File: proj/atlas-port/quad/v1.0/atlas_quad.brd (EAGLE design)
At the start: 123.2 x 21.6 mm, 30 parts, among them J1 Atlas Stamp, J2 5227161-9, J3 I2C-HEADER, J4 5227161-9, J5 Atlas Stamp, J6 I2C-HEADER, U1 ISO1540, U2 RM-3.33.3S, U3 ISO1540, U4 RM-3.33.3S

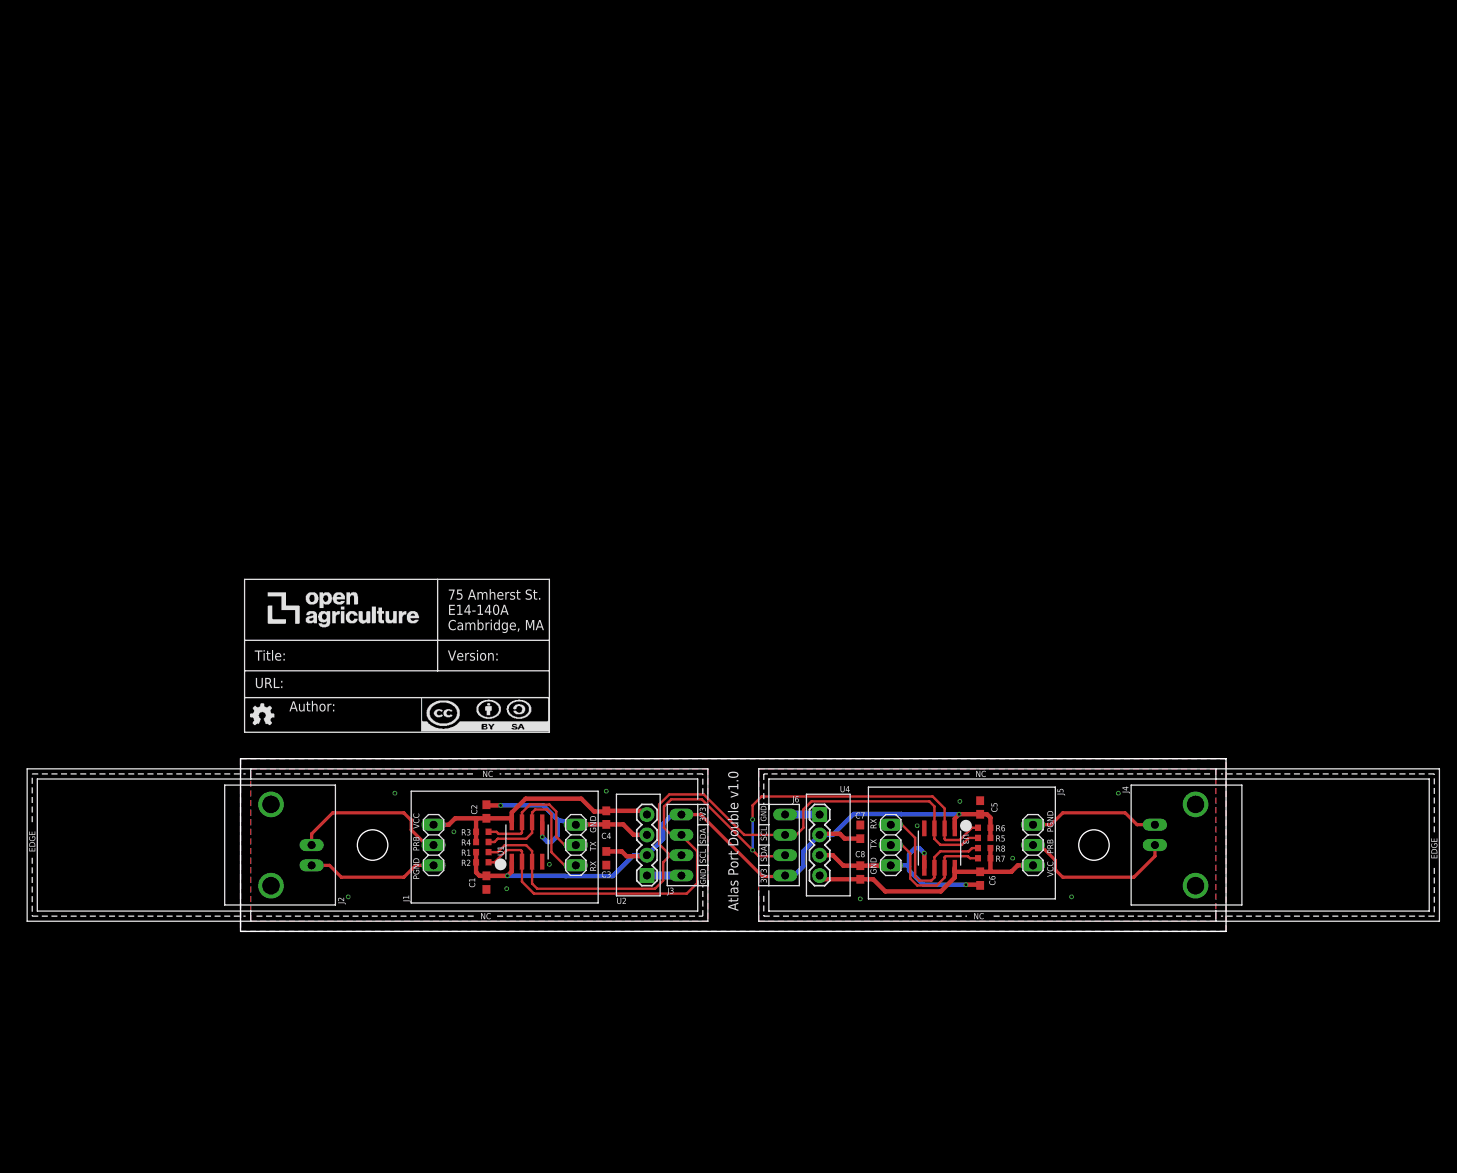
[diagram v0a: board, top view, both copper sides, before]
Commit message: added atlas sensor port quad v1.0
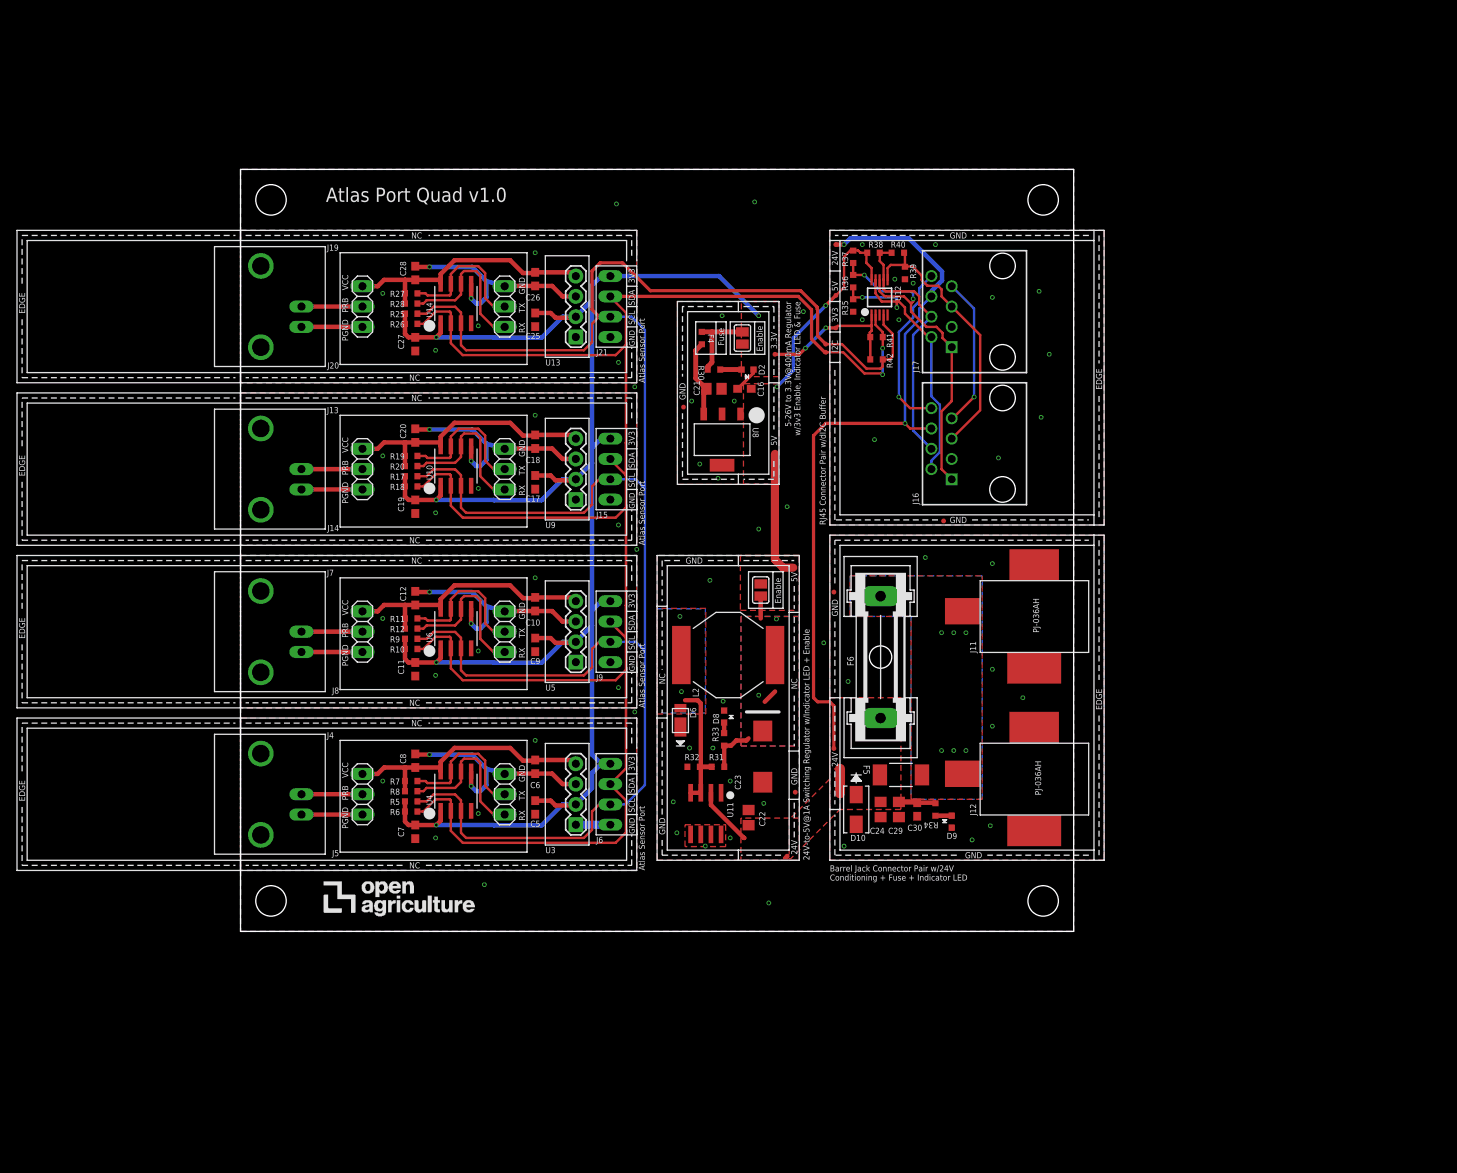
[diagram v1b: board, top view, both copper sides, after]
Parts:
- removed C1, C2, C3, C4: 0.1uF, openag-capacitors:C0603
- removed J1: Atlas Stamp, openag-connectors:ATLAS-STAMP
- removed J2: 5227161-9, openag-connectors:BNC
- removed J3: I2C-HEADER, openag-connectors:OPENAG-I2C-HEADER
- removed R1, R2, R3, R4: 1K, openag-resistors:RC0603N
- removed U1: ISO1540, openag-isolators:D8
- removed U2: RM-3.33.3S, openag-isolators:SIP4
- added C10, C11, C12, C16, C17, C18, C19, C20, C25, C26, C27, C28, C30, C9: 0.1uF, openag-capacitors:C0603
- added C21, C24: 10uF, openag-capacitors:C0805
- added C22: 15uF, openag-capacitors:C0805
- added C23: 220uF, openag-capacitors:CT7343
- added C29: 4.7uF, openag-capacitors:C0805
- added D10: SMAJ26A, openag-diodes:SMA
- added D2, D8, D9: APT1608, openag-diodes:CHIPLED_0603
- added D6: SBR2A40P1-7, openag-diodes:POWERDI123
- added F4: 0448.400MR, openag-fuses:0603
- added F5: SST 7, openag-fuses:SS
- added F6: (no value), fuse:GSH15
- added J11, J12: PJ-036AH, openag-connectors:PJ-036AH
- added J13, J19, J7: 5227161-9, openag-connectors:BNC
- added J14, J20, J8: Atlas Stamp, openag-connectors:ATLAS-STAMP
- added J15, J21, J9: I2C-HEADER, openag-connectors:OPENAG-I2C-HEADER
- added J16, J17: 54602-908LF, openag_connector:OPENAG-V1-RJ45
- added L2: 68uH, openag-inductors:UP2B
- added R10, R11, R12, R17, R18, R19, R20, R25, R26, R27, R28, R9: 1K, openag-resistors:RC0603N
- added R30, R33, R34: 100, openag-resistors:RC0603N
- added R31: 3.01K, openag-resistors:RC0603N
- added R32: 976 Ohm, openag-resistors:RC0603N
- added R35, R37, R38, R39: 600, openag-resistors:RC0603N
- added R36, R40: 120, openag-resistors:RC0603N
- added R41, R42: 10K, openag-resistors:RC0603N
- added SJ1, SJ4: (no value), openag-connectors:SOLDERJUMPER_REFLOW_NOPASTE
- added TP1, TP10, TP11, TP12, TP13, TP14, TP15, TP16, TP17, TP18, TP2, TP3, TP8, TP9: TPTP06R, openag-testpads:TP06R
- added U$1, U$4: (no value), openag-frames:OPENAG-CORNER-MOUNTING-HOLE
- added U10, U14, U6: ISO1540, openag-isolators:D8
- added U11: MIC4680YM-TR, openag-regulators:SOIC8
- added U12: PCA9615DPJ, openag-buffers:SOP50P490X110-10N
- added U13, U5, U9: RM-3.33.3S, openag-isolators:SIP4
- added U8: LM2937IMP3.3NOPB, openag-regulators:MP04A
- U3: value ISO1540 -> RM-3.33.3S; device openag-isolators:D8 -> openag-isolators:SIP4
- U4: value RM-3.33.3S -> ISO1540; device openag-isolators:SIP4 -> openag-isolators:D8
- moved J4 117.0 mm to (2.54, 17.1), turned to 90 degrees
- moved R7 72.3 mm to (21.3, 18.8), turned to 180 degrees
- moved R8 72.0 mm to (21.3, 17.5), turned to 180 degrees
- moved R5 71.8 mm to (21.3, 16.3), turned to 180 degrees
- moved R6 71.7 mm to (21.3, 15.0), turned to 180 degrees
- moved J5 66.3 mm to (24.1, 17.1), turned to 180 degrees
- moved FRAME1 57.8 mm to (52.8, 49.5), flipped to the bottom, turned to 90 degrees
- moved C6 57.4 mm to (36.8, 20.6)
- moved C8 57.4 mm to (21.8, 21.3)
- moved C5 55.6 mm to (36.8, 15.5), turned to 270 degrees
- moved C7 55.6 mm to (21.8, 12.4), turned to 270 degrees
- moved U$5 49.3 mm to (10.4, 2.29), flipped to the top, turned to 0 degrees
- moved U3 45.6 mm to (41.9, 13.3), turned to 90 degrees
- moved U4 45.6 mm to (26.9, 17.5), turned to 90 degrees
- moved J6 21.3 mm to (47.0, 17.1), turned to 90 degrees
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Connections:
- new net +24V: C22.1, C24.1, C29.1, C30.1, D10.1, F5.2, F6.2, J16.24V(6), J17.24V(6), R34.2, TP10.TP, TP12.TP, TP18.TP, U11.2
- new net +5V: C16.1, R37.1, R38.2, SJ4.2, TP17.TP, TP2.TP, TP8.TP, U12.10, U8.1
- new net 24V_IN: F5.1, F6.1, J11.1, J12.1
- new net DSCLM: J16.DSCLM(5), J17.DSCLM(5), R39.2, R40.1, U12.6
- new net DSCLP: J16.DSCLP(4), J17.DSCLP(4), R38.1, R40.2, U12.7
- new net DSDAM: J16.DSDAM(2), J17.DSDAM(2), R35.1, R36.2, U12.9
- new net DSDAP: J16.DSDAP(1), J17.DSDAP(1), R36.1, R37.2, U12.8
- new net ISO_3V3_3: C18.1, C20.1, J14.4, R19.2, R20.2, U10.8, U9.4
- new net ISO_3V3_4: C26.1, C28.1, J20.4, R27.2, R28.2, U13.4, U14.8
- new net ISO_GND_3: C18.2, C20.2, J14.3, U10.5, U9.3
- new net ISO_GND_4: C26.2, C28.2, J20.3, U13.3, U14.5
- new net ISO_SCL_3: J14.1, R20.1, U10.6
- new net ISO_SCL_4: J20.1, R28.1, U14.6
- new net ISO_SDA_3: J14.2, R19.1, U10.7
- new net ISO_SDA_4: J20.2, R27.1, U14.7
- new net N$11: D6.+, L2.1, R31.1, R32.2, U11.3, U11.4
- new net N$27: D8.A, R33.1
- new net N$45: C23.+, L2.2, R31.2, R33.2, SJ4.1
- new net N$46: D9.A, R34.1
- new net N$6: D2.A, R30.1
- new net N$8: C21.1, F4.1, U8.3
- new net PGND_3: J13.GND, J14.6
- new net PGND_4: J19.GND, J20.6
- new net PRB_3: J13.S, J14.5
- new net PRB_4: J19.S, J20.5
- new net REG_3V3_400MA: F4.2, R30.2, SJ1.1
- new net USBM: J16.USBM(8), J17.USBM(8)
- new net USBP: J16.USBP(7), J17.USBP(7)
- net +3V3: now also C11.1, C17.1, C19.1, C25.1, C27.1, C9.1, J15.3V3, J21.3V3, J9.3V3, R10.2, R17.2, R18.2, R25.2, R26.2, R41.2, R42.2, R9.2, SJ1.2, TP15.TP, TP3.TP, U10.1, U12.1, U13.2, U14.1, U3.2, U4.1, U5.2, U6.1, U9.2; no longer C1.1, C3.1, J3.3V3, R1.2, R2.2, U1.1, U2.2, U3.1, U4.2
- net GND: now also C11.2, C16.2, C17.2, C19.2, C21.2, C22.2, C23.-, C24.2, C25.2, C27.2, C29.2, C30.2, C9.2, D10.2, D2.C, D6.-, D8.C, D9.C, J11.2, J11.3, J12.2, J12.3, J15.GND, J16.GND(3), J17.GND(3), J21.GND, J9.GND, R32.1, R35.2, R39.1, TP1.TP, TP11.TP, TP16.TP, TP9.TP, U10.4, U11.1, U11.5, U11.6, U11.7, U11.8, U12.5, U13.1, U14.4, U3.1, U4.4, U5.1, U6.4, U8.2, U8.4, U9.1; no longer C1.2, C3.2, J3.GND, U1.4, U2.1, U3.4, U4.1
- net ISO_3V3_1: now also C6.1, C8.1, J5.4, R7.2, R8.2, U3.4, U4.8; no longer C2.1, C4.1, J1.4, R3.2, R4.2, U1.8, U2.4
- net ISO_3V3_2: now also C10.1, C12.1, J8.4, R11.2, R12.2, U5.4, U6.8; no longer C6.1, C8.1, J5.4, R7.2, R8.2, U3.8, U4.4
- net ISO_GND_1: now also C6.2, C8.2, J5.3, U3.3, U4.5; no longer C2.2, C4.2, J1.3, U1.5, U2.3
- net ISO_GND_2: now also C10.2, C12.2, J8.3, U5.3, U6.5; no longer C6.2, C8.2, J5.3, U3.5, U4.3
- net ISO_SCL_1: now also J5.1, R8.1, U4.6; no longer J1.1, R4.1, U1.6
- net ISO_SCL_2: now also J8.1, R12.1, U6.6; no longer J5.1, R8.1, U3.6
- net ISO_SDA_1: now also J5.2, R7.1, U4.7; no longer J1.2, R3.1, U1.7
- net ISO_SDA_2: now also J8.2, R11.1, U6.7; no longer J5.2, R7.1, U3.7
- net PGND_1: now also J4.GND, J5.6; no longer J1.6, J2.GND
- net PGND_2: now also J7.GND, J8.6; no longer J4.GND, J5.6
- net PRB_1: now also J4.S, J5.5; no longer J1.5, J2.S
- net PRB_2: now also J7.S, J8.5; no longer J4.S, J5.5
- net SCL: now also J15.SCL, J21.SCL, J9.SCL, R17.1, R25.1, R42.1, R9.1, TP13.TP, U10.3, U12.4, U14.3, U4.3, U6.3; no longer J3.SCL, R1.1, U1.3, U3.3
- net SDA: now also J15.SDA, J21.SDA, J9.SDA, R10.1, R18.1, R26.1, R41.1, TP14.TP, U10.2, U12.2, U14.2, U4.2, U6.2; no longer J3.SDA, R2.1, U1.2, U3.2
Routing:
- net SCL: track 89.6 -> 263.9 mm
- net +3V3: track 96.6 -> 255.2 mm, vias 2 -> 7
- net SDA: track 101.6 -> 250.1 mm
- net +24V: track 0.00 -> 108.5 mm, vias 0 -> 2
- net DSDAP: track 0.00 -> 43.2 mm, vias 0 -> 2
- net +5V: track 0.00 -> 42.7 mm, vias 0 -> 2
- net DSDAM: track 0.00 -> 38.1 mm, vias 0 -> 2
- net DSCLM: track 0.00 -> 33.9 mm
- net ISO_3V3_3: track 0.00 -> 33.3 mm
- net ISO_3V3_4: track 0.00 -> 33.3 mm
- net DSCLP: track 0.00 -> 32.7 mm
- net ISO_GND_3: track 0.00 -> 27.8 mm, vias 0 -> 2
- net ISO_GND_4: track 0.00 -> 27.8 mm, vias 0 -> 2
- net USBM: track 0.00 -> 21.4 mm, vias 0 -> 1
- net ISO_SCL_3: track 0.00 -> 19.8 mm
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- added copper zone on layer 1, net +24V
- added copper zone on layer 1, net +3V3
- added copper zone on layer 1, net +5V
- added copper zone on layer 1, net 24V_IN
- added copper zone on layer 16, net 24V_IN
- added copper zone on layer 1, net N$11
- added copper zone on layer 16, net N$11
- added copper zone on layer 1, net N$45
- added copper zone on layer 16, net N$45
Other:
- board size 123.2 x 21.6 mm -> 104.1 x 95.2 mm
- board text added: "24V"
- board text added: "24V-to-5V@1A Switching Regulator w/Indicator LED + Enable"
- board text added: "3.3V"
- board text added: "3V3"
- board text added: "5-26V to 3.3V@400mA Regulator w/3v3 Enable, Indicator LED & Fuse"
- board text added: "5V"
- board text added: "Atlas Port Quad v1.0"
- board text added: "Atlas Sensor Port"
- board text added: "Barrel Jack Connector Pair w/24V Conditioning + Fuse + Indicator LED"
- board text added: "Enable"
- board text added: "Fuse"
- board text added: "GND"
- board text added: "I2C"
- board text added: "RJ45 Connector Pair w/dI2C Buffer"
- board text removed: "Atlas Port Double v1.0"

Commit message: updated atlas port quad v1.0 manufacturing files
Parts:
- F5: value SST 7 -> SST7
- F6: device fuse:GSH15 -> openag-fuses:GSH15
- J16, J17: device openag_connector:OPENAG-V1-RJ45 -> openag-connectors:OPENAG-V1-RJ45
- U11: value MIC4680YM-TR -> MIC4680
- U12: value PCA9615DPJ -> PCA9615
- U8: value LM2937IMP3.3NOPB -> LM2937

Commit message: added photon quad v1.0 at 90%
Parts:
- removed C29: 4.7uF, openag-capacitors:C0805
- removed C30, C8: 0.1uF, openag-capacitors:C0603
- removed D10: SMAJ26A, openag-diodes:SMA
- removed D8, D9: APT1608, openag-diodes:CHIPLED_0603
- removed F4: 0448.400MR, openag-fuses:0603
- removed F5: SST7, openag-fuses:SS
- removed F6: (no value), openag-fuses:GSH15
- removed FRAME1: (no value), openag-frames:DOCFIELD
- removed J11, J12: PJ-036AH, openag-connectors:PJ-036AH
- removed J16, J17: 54602-908LF, openag-connectors:OPENAG-V1-RJ45
- removed R20: 1K, openag-resistors:RC0603N
- removed R30, R33, R34: 100, openag-resistors:RC0603N
- removed R31: 3.01K, openag-resistors:RC0603N
- removed R32: 976 Ohm, openag-resistors:RC0603N
- removed R35, R37, R38, R39: 600, openag-resistors:RC0603N
- removed R36, R40: 120, openag-resistors:RC0603N
- removed R41, R42: 10K, openag-resistors:RC0603N
- removed SJ4: (no value), openag-connectors:SOLDERJUMPER_REFLOW_NOPASTE
- removed TP16: TPTP06R, openag-testpads:TP06R
- removed U11: MIC4680, openag-regulators:SOIC8
- added C1, C14, C2, C3, C4: 0.1uF, openag-capacitors:C0603
- added C15: 10uF, openag-capacitors:C0805
- added D1, D4: APT1608, openag-diodes:CHIPLED_0603
- added D3: SMAJ26A, openag-diodes:SMA
- added F1, F2: SSQ5, openag-fuses:SS
- added J1: 5227161-9, openag-connectors:BNC-5227161
- added J10: 54602-908LF, openag-connectors:RJ45-DI2C-USB-54602-908LF
- added J2: I2C-HEADER, openag-connectors:HEADER-I2C
- added J3: ATLAS-STAMP, openag-connectors:ATLAS-STAMP
- added R1, R2, R23, R24: 2.2k, openag-resistors:RC0603N
- added R13: 1K, openag-resistors:RC0603N
- added R14, R15, R16, R3: 600, openag-resistors:RC0603N
- added R21, R22: 100, openag-resistors:RC0603N
- added R4: 120, openag-resistors:RC0603N
- added TP19, TP20, TP28, TP29, TP30, TP31, TP32, TP4, TP5, TP58, TP6, TP7, TP71, TP72, TP73: TPTP04R, openag-testpads:TP04R
- added TP23, TP24, TP25: TPTP06R, openag-testpads:TP06R
- added U$6: TITLE, openag-frames:TITLE
- added U$8: (no value), openag-frames:LOGO-900X300
- added U1: ISO1540, openag-isolators:D8
- added U2: RM-3.33.3S, openag-isolators:RM3.33.3S-SIP4
- added U7: LM2937-3.3V, openag-regulators:MP04A
- C20, C5: value 0.1uF -> 10uF; device openag-capacitors:C0603 -> openag-capacitors:C0805
- C22: value 15uF -> 10uF
- C23: value 220uF -> 0.1uF; device openag-capacitors:CT7343 -> openag-capacitors:C0603
- C24: value 10uF -> 0.1uF; device openag-capacitors:C0805 -> openag-capacitors:C0603
- C28, C6: value 0.1uF -> 4.7uF; device openag-capacitors:C0603 -> openag-capacitors:C0805
- D6: value SBR2A40P1-7 -> APT1608; device openag-diodes:POWERDI123 -> openag-diodes:CHIPLED_0603
- J13, J19, J7: value 5227161-9 -> ATLAS-STAMP; device openag-connectors:BNC -> openag-connectors:ATLAS-STAMP
- J14, J20, J8: value Atlas Stamp -> I2C-HEADER; device openag-connectors:ATLAS-STAMP -> openag-connectors:HEADER-I2C
- J15, J21, J9: value I2C-HEADER -> 5227161-9; device openag-connectors:OPENAG-I2C-HEADER -> openag-connectors:BNC-5227161
- J4: value 5227161-9 -> PJ-036AH; device openag-connectors:BNC -> openag-connectors:BARREL-JACK-PJ-036AH
- J5: value Atlas Stamp -> PJ-036AH; device openag-connectors:ATLAS-STAMP -> openag-connectors:BARREL-JACK-PJ-036AH
- J6: value I2C-HEADER -> 54602-908LF; device openag-connectors:OPENAG-I2C-HEADER -> openag-connectors:RJ45-DI2C-USB-54602-908LF
- L2: value 68uH -> 33uH; device openag-inductors:UP2B -> openag-inductors:29333C
- R10, R18, R19: value 1K -> 120
- R11, R12: value 1K -> 10K
- R17, R7, R8, R9: value 1K -> 600
- R25: value 1K -> 0 OHM
- R26: value 1K -> 100
- R27, R28, R5, R6: value 1K -> 2.2k
- SJ1: device openag-connectors:SOLDERJUMPER_REFLOW_NOPASTE -> openag-connectors:EMI-BYPASS
- TP1, TP10, TP11, TP12, TP13, TP14, TP15, TP17, TP18, TP2, TP3, TP8, TP9: value TPTP06R -> TPTP04R; device openag-testpads:TP06R -> openag-testpads:TP04R
- U$1, U$2, U$3, U$4: device openag-frames:OPENAG-CORNER-MOUNTING-HOLE -> openag-frames:CORNER-150
- U$5: value (none) -> AUTHOR; device openag-frames:OPENAG-LOGO-750-MIL -> openag-frames:AUTHOR
- U12: value PCA9615 -> PHOTONH; device openag-buffers:SOP50P490X110-10N -> openag-microcontrollers:PHOTON
- U13, U5, U9: device openag-isolators:SIP4 -> openag-isolators:RM3.33.3S-SIP4
- U3: value RM-3.33.3S -> PCA9615; device openag-isolators:SIP4 -> openag-buffers:SOP50P490X110-10N
- U4: value ISO1540 -> PCA9615; device openag-isolators:D8 -> openag-buffers:SOP50P490X110-10N
- U8: value LM2937 -> R-78E5.0-1.0; device openag-regulators:MP04A -> openag-regulators:R-78E5.0-1.0
- moved U$2 136.7 mm to (95.2, 105.4), turned to 180 degrees
- moved U$1 125.8 mm to (95.2, 5.08), turned to 90 degrees
- moved U$5 105.6 mm to (99.1, 59.7), turned to 90 degrees
- moved J4 99.8 mm to (61.0, 98.1), turned to 270 degrees
- moved J5 97.7 mm to (78.7, 98.1), turned to 270 degrees
- moved U$4 96.3 mm to (5.08, 105.4), turned to 270 degrees
- moved U$3 95.3 mm to (5.08, 5.08), turned to 0 degrees
- moved TP10 90.1 mm to (47.5, 97.1)
- moved J6 87.5 mm to (21.6, 100.9), turned to 180 degrees
- moved C7 84.5 mm to (69.3, 82.3)
- moved TP9 83.6 mm to (47.5, 98.1)
- moved TP12 82.9 mm to (47.5, 101.4), turned to 270 degrees
- moved J21 80.3 mm to (19.7, 2.54), turned to 180 degrees
- moved C5 76.3 mm to (73.7, 82.3)
- moved U3 76.2 mm to (23.1, 87.2), turned to 180 degrees
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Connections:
- removed net 24V_IN: F5.1, F6.1, J11.1, J12.1
- removed net DSCLM: J16.DSCLM(5), J17.DSCLM(5), R39.2, R40.1, U12.6
- removed net DSCLP: J16.DSCLP(4), J17.DSCLP(4), R38.1, R40.2, U12.7
- removed net DSDAM: J16.DSDAM(2), J17.DSDAM(2), R35.1, R36.2, U12.9
- removed net DSDAP: J16.DSDAP(1), J17.DSDAP(1), R36.1, R37.2, U12.8
- removed net N$27: D8.A, R33.1
- removed net N$45: C23.+, L2.2, R31.2, R33.2, SJ4.1
- removed net N$46: D9.A, R34.1
- removed net REG_3V3_400MA: F4.2, R30.2, SJ1.1
- new net 24V_EMI: C15.1, L2.2, SJ1.2, U8.1
- new net 24V_IN1: F2.1, J5.1
- new net 24V_IN2: F1.1, J4.1
- new net DSCLM_1: J6.DSCLM(5), R10.1, R9.2, U3.6
- new net DSCLM_2: J10.DSCLM(5), R16.2, R18.1, U4.6
- new net DSCLP_1: J6.DSCLP(4), R10.2, R8.1, U3.7
- new net DSCLP_2: J10.DSCLP(4), R17.1, R18.2, U4.7
- new net DSDAM_1: J6.DSDAM(2), R3.1, R4.2, U3.9
- new net DSDAM_2: J10.DSDAM(2), R14.1, R19.2, U4.9
- new net DSDAP_1: J6.DSDAP(1), R4.1, R7.2, U3.8
- new net DSDAP_3: J10.DSDAP(1), R15.2, R19.1, U4.8
- new net N$4: R25.2, U12.1
- new net N$5: D1.A, R13.1
- new net VBAT: U12.22
- net +24V: now also C21.1, C5.1, C6.1, C7.1, D3.1, F1.2, F2.2, J10.24V(6), J6.24V(6), L2.1, R13.2, R21.2, SJ1.1, TP11.1, TP17.1, TP20.1, TP24.TP, TP4.1; no longer C22.1, C24.1, C29.1, C30.1, D10.1, F5.2, F6.2, J16.24V(6), J17.24V(6), R34.2, TP10.TP, TP12.TP, TP18.TP, U11.2
- net +3V3: now also C1.1, C16.1, C18.1, C22.1, C23.1, C24.1, C26.1, C28.1, C3.1, J14.3V3, J2.3V3, J20.3V3, J8.3V3, R11.2, R12.2, TP1.1, TP28.1, TP31.1, TP71.1, TP9.1, U1.1, U12.24, U2.2, U3.1, U7.3; no longer C17.1, C19.1, C25.1, C27.1, C5.1, C7.1, J15.3V3, J21.3V3, J6.3V3, J9.3V3, R10.2, R17.2, R18.2, R25.2, R41.2, R42.2, R5.2, R6.2, R9.2, SJ1.2, TP15.TP, TP3.TP, U12.1, U3.2
- net +5V: now also C14.1, C20.1, R15.1, R17.2, R22.2, R25.1, R7.1, R8.2, TP10.1, TP2.1, TP23.TP, TP29.1, U3.10, U4.10, U7.1, U8.3; no longer C16.1, R37.1, R38.2, SJ4.2, TP17.TP, TP2.TP, TP8.TP, U12.10, U8.1
- net GND: now also C1.2, C14.2, C15.2, C18.2, C20.2, C23.2, C26.2, C28.2, C3.2, C6.2, D1.C, D3.2, D4.C, D6.C, J10.GND(3), J14.GND, J2.GND, J20.GND, J4.2, J4.3, J5.2, J5.3, J6.GND(3), J8.GND, R14.2, R16.1, R3.2, R9.1, TP12.1, TP15.1, TP18.1, TP19.1, TP25.TP, TP3.1, TP30.1, TP32.1, TP72.1, U1.4, U12.2, U12.21, U2.1, U3.5, U4.5, U7.2, U7.4; no longer C17.2, C19.2, C23.-, C25.2, C27.2, C29.2, C30.2, D10.2, D6.-, D8.C, D9.C, J11.2, J11.3, J12.2, J12.3, J15.GND, J16.GND(3), J17.GND(3), J21.GND, J6.GND, J9.GND, R32.1, R35.2, R39.1, TP1.TP, TP11.TP, TP16.TP, TP9.TP, U11.1, U11.5, U11.6, U11.7, U11.8, U12.5, U3.1, U4.4, U8.4
- net ISO_3V3_1: now also C2.1, C4.1, J3.4, R1.2, R2.2, U1.8, U2.4; no longer C6.1, C8.1, J5.4, R7.2, R8.2, U3.4, U4.8
- net ISO_3V3_2: now also J7.4, R5.2, R6.2; no longer J8.4, R11.2, R12.2
- net ISO_3V3_3: now also C17.1, C19.1, J13.4, R23.2, R24.2; no longer C18.1, C20.1, J14.4, R19.2, R20.2
- net ISO_3V3_4: now also C25.1, C27.1, J19.4; no longer C26.1, C28.1, J20.4
- net ISO_GND_1: now also C2.2, C4.2, J3.3, U1.5, U2.3; no longer C6.2, C8.2, J5.3, U3.3, U4.5
- net ISO_GND_2: now also J7.3; no longer J8.3
- net ISO_GND_3: now also C17.2, C19.2, J13.3; no longer C18.2, C20.2, J14.3
- net ISO_GND_4: now also C25.2, C27.2, J19.3; no longer C26.2, C28.2, J20.3
- net ISO_SCL_1: now also J3.1, R2.1, U1.6; no longer J5.1, R8.1, U4.6
- net ISO_SCL_2: now also J7.1, R5.1; no longer J8.1, R12.1
- net ISO_SCL_3: now also J13.1, R23.1; no longer J14.1, R20.1
- net ISO_SCL_4: now also J19.1, R27.1; no longer J20.1, R28.1
- net ISO_SDA_1: now also J3.2, R1.1, U1.7; no longer J5.2, R7.1, U4.7
- net ISO_SDA_2: now also J7.2, R6.1; no longer J8.2, R11.1
- net ISO_SDA_3: now also J13.2, R24.1; no longer J14.2, R19.1
- net ISO_SDA_4: now also J19.2, R28.1; no longer J20.2, R27.1
- net N$11: now also D6.A, R26.1; no longer D6.+, L2.1, R31.1, R32.2, U11.3, U11.4
- net N$6: now also R21.1; no longer R30.1
- net N$8: now also D4.A, R22.1; no longer C21.1, F4.1, U8.3
- net PGND_1: now also J1.GND, J3.6; no longer J4.GND, J5.6
- net PGND_2: now also J7.6, J9.GND; no longer J7.GND, J8.6
- net PGND_3: now also J13.6, J15.GND; no longer J13.GND, J14.6
- net PGND_4: now also J19.6, J21.GND; no longer J19.GND, J20.6
- net PRB_1: now also J1.S, J3.5; no longer J4.S, J5.5
- net PRB_2: now also J7.5, J9.S; no longer J7.S, J8.5
- net PRB_3: now also J13.5, J15.S; no longer J13.S, J14.5
- net PRB_4: now also J19.5, J21.S; no longer J19.S, J20.5
- net SCL: now also J14.SCL, J2.SCL, J20.SCL, J8.SCL, R12.1, TP13.1, TP58.1, TP6.1, U1.3, U12.14, U3.4, U4.4; no longer J15.SCL, J21.SCL, J6.SCL, J9.SCL, R17.1, R25.1, R42.1, R5.1, R9.1, TP13.TP, U12.4, U4.3
- net SDA: now also J14.SDA, J2.SDA, J20.SDA, J8.SDA, R11.1, TP14.1, TP5.1, TP73.1, U1.2, U12.13, U3.2; no longer J15.SDA, J21.SDA, J6.SDA, J9.SDA, R10.1, R18.1, R26.1, R41.1, R6.1, TP14.TP, U12.2
- net USBM: now also J10.USBM(8), J6.USBM(8), TP8.1; no longer J16.USBM(8), J17.USBM(8)
- net USBP: now also J10.USBP(7), J6.USBP(7), TP7.1; no longer J16.USBP(7), J17.USBP(7)
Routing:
- net +3V3: track 255.2 -> 428.3 mm, vias 7 -> 8
- net +5V: track 42.7 -> 171.9 mm, vias 2 -> 9
- net SDA: track 250.1 -> 320.4 mm, vias 2 -> 0
- net SCL: track 263.9 -> 325.3 mm, vias 0 -> 6
- net DSDAP: track 43.2 -> 0.00 mm, vias 2 -> 0
- net DSDAM: track 38.1 -> 0.00 mm, vias 2 -> 0
- net DSCLM: track 33.9 -> 0.00 mm
- net DSCLP: track 32.7 -> 0.00 mm
- net +24V: track 108.5 -> 82.7 mm, vias 2 -> 33
- net USBP: track 18.9 -> 41.0 mm, vias 1 -> 0
- net USBM: track 21.4 -> 39.4 mm, vias 1 -> 0
- net DSDAP_1: track 0.00 -> 16.7 mm
- net DSDAP_3: track 0.00 -> 16.5 mm
- net 24V_EMI: track 0.00 -> 15.9 mm
- net DSDAM_2: track 0.00 -> 14.7 mm
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- added copper zone on layer 16, net +24V
- added copper zone on layer 1, net 24V_IN1
- added copper zone on layer 16, net 24V_IN1
- added copper zone on layer 1, net 24V_IN2
- added copper zone on layer 16, net 24V_IN2
- removed copper zone on layer 1, net 24V_IN
- removed copper zone on layer 16, net 24V_IN
- removed copper zone on layer 1, net N$11
- removed copper zone on layer 16, net N$11
- removed copper zone on layer 1, net N$45
- removed copper zone on layer 16, net N$45
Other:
- board size 104.1 x 95.2 mm -> 100.3 x 110.5 mm
- board text added: "24V to 5V@1A Switching Regulator w/Optional EMI Filter + Indicator LED"
- board text added: "5V Enable"
- board text added: "5V to 3.3V@400mA Linear Regulator w/ LED"
- board text added: "Atlas Sensor Port w/Header"
- board text added: "Barrel Jack Connector Pair w/24V Conditioning + Fuse + LED"
- board text added: "Description: Connects x4 Atlas probes to the nervous system board via RJ45-dI2C comms. Includes photon headers for optional standalone control."
- board text added: "Particle Photon"
- board text added: "RJ45 Connector Pair w/dI2C Buffer + LED"
- board text added: "SCL"
- board text added: "SDA"
- board text added: "USBM"
- board text added: "USBP"
- board text added: "Want to get involved? - Chat with us: forum.openag.media.mit.edu - Follow our twitter: @MITOpenAg - Make a pull request: @OpenAgInitiative"
- board text removed: "24V-to-5V@1A Switching Regulator w/Indicator LED + Enable"
- board text removed: "5-26V to 3.3V@400mA Regulator w/3v3 Enable, Indicator LED & Fuse"
- board text removed: "Atlas Port Quad v1.0"
- board text removed: "Atlas Sensor Port"
- board text removed: "Barrel Jack Connector Pair w/24V Conditioning + Fuse + Indicator LED"
- board text removed: "Enable"
- board text removed: "Fuse"
- board text removed: "I2C"
- board text removed: "RJ45 Connector Pair w/dI2C Buffer"

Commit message: added atlas port quad v1.0 and air sensor node v1.1
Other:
- board text added: "Particle Photon w/I2C Leads + 5V Enable"
- board text removed: "Particle Photon"
